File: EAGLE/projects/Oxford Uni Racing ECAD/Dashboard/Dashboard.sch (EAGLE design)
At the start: 21 parts, among them J1 T821108A1S100CEU, J2 CAN_OUT, J3 PWR_CAN, J4 DISPL, J6 BUTTONS, J7 BUTTONS, K1 EC2-12NU, K2 EC2-12NU, X2 D-SUB9-H2M09ST

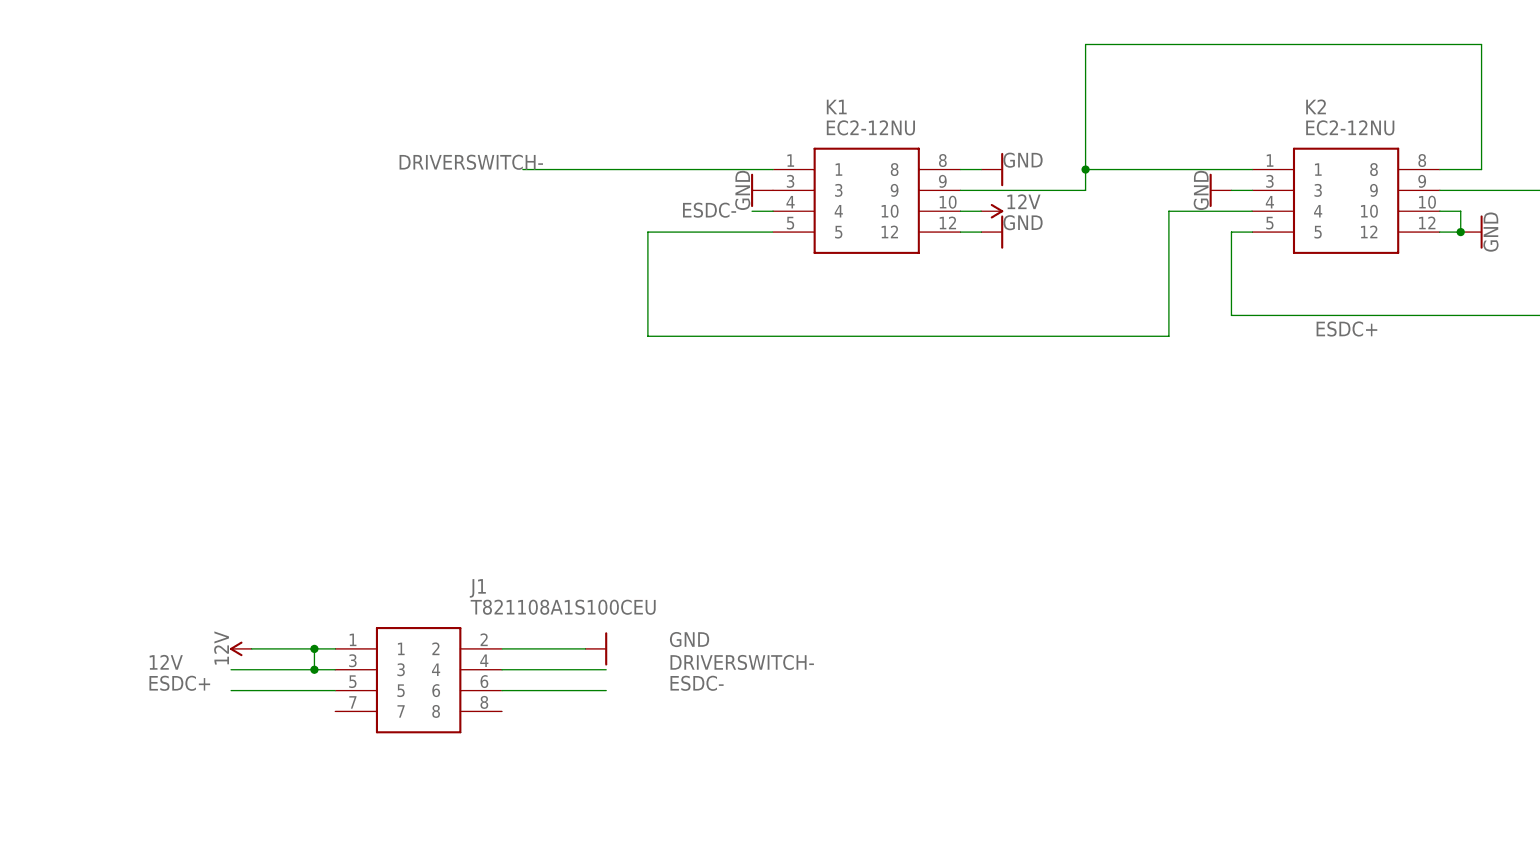
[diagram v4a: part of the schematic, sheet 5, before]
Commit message: fixed wiring of TS_Latch on dashboard
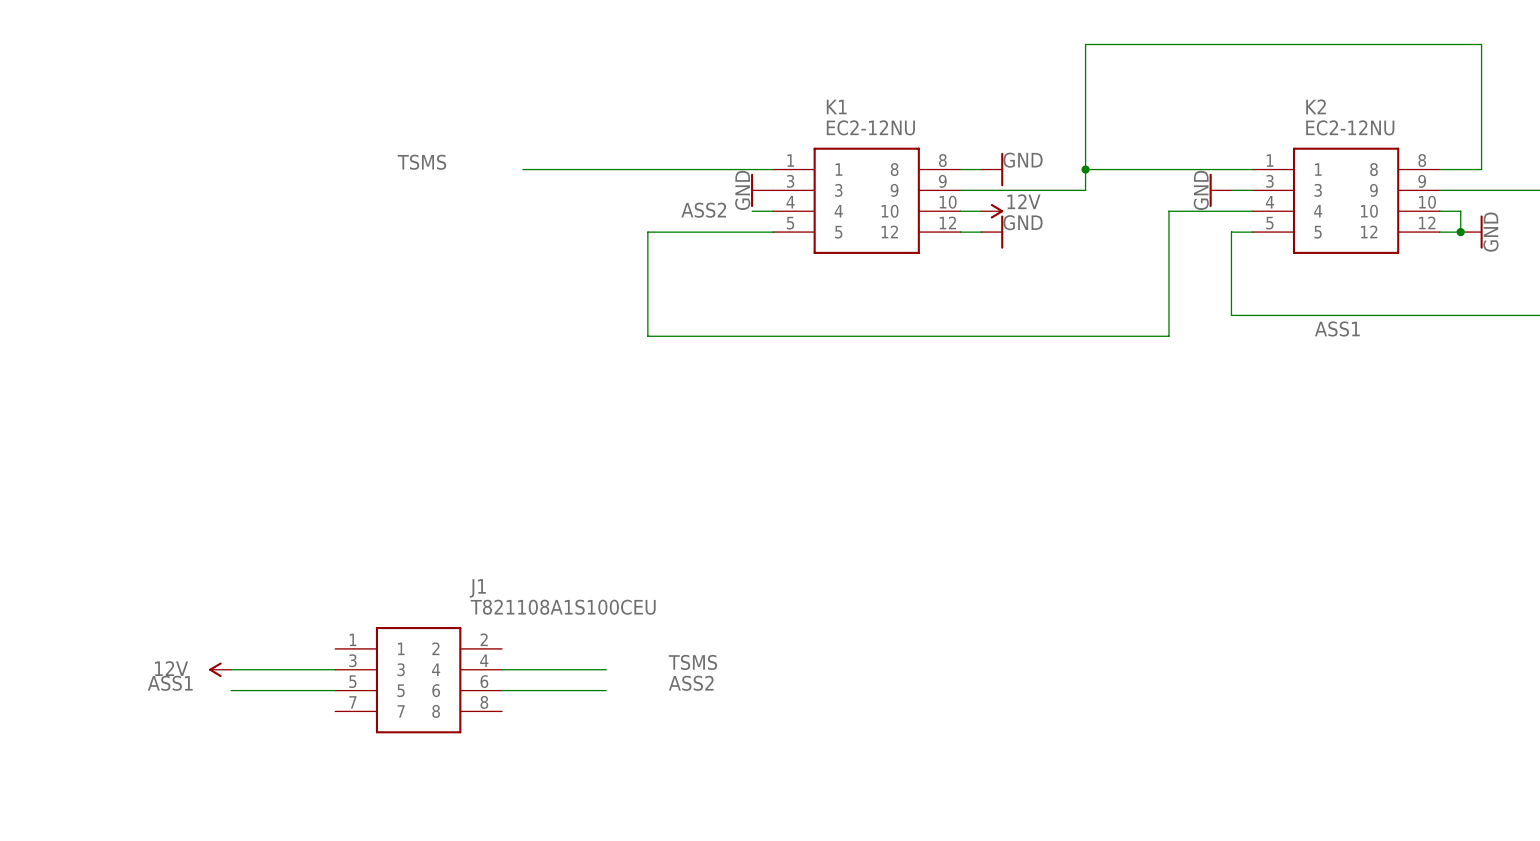
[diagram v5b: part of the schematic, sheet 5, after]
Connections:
- net DRIVERSWITCH- renamed TSMS
- net ESDC+ renamed ASS1
- net ESDC- renamed ASS2
- net 12V: no longer J1.1
- net GND: no longer J1.2
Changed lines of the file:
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@@
 <part name="GND12" library="SparkFun-PowerSymbols" library_urn="urn:adsk.eagle:library:530" deviceset="GND" device=""/>
 <part name="GND13" library="SparkFun-PowerSymbols" library_urn="urn:adsk.eagle:library:530" deviceset="GND" device=""/>
-<part name="GND14" library="SparkFun-PowerSymbols" library_urn="urn:adsk.eagle:library:530" deviceset="GND" device=""/>
-<part name="SUPPLY33" library="SparkFun-PowerSymbols" library_urn="urn:adsk.eagle:library:530" deviceset="12V" device=""/>
 <part name="SUPPLY1" library="SparkFun-PowerSymbols" library_urn="urn:adsk.eagle:library:530" deviceset="12V" device=""/>
 <part name="X2" library="con-thomas-betts" library_urn="urn:adsk.eagle:library:191" deviceset="D-SUB9-" device="H2M09ST" package3d_urn="urn:adsk.eagle:package:10567/1"/>
@@
 <part name="SUPPLY19" library="SparkFun-PowerSymbols" library_urn="urn:adsk.eagle:library:530" deviceset="3.3V" device=""/>
 <part name="GND4" library="SparkFun-PowerSymbols" library_urn="urn:adsk.eagle:library:530" deviceset="GND" device=""/>
+<part name="SUPPLY33" library="SparkFun-PowerSymbols" library_urn="urn:adsk.eagle:library:530" deviceset="12V" device=""/>
 </parts>
 <sheets>
@@
 <attribute name="VALUE" x="178.054" y="81.28" size="1.778" layer="96" rot="R90" align="top-center"/>
 </instance>
-<instance part="GND14" gate="1" x="71.12" y="30.48" smashed="yes" rot="R90">
-<attribute name="VALUE" x="81.28" y="30.734" size="1.778" layer="96" rot="R180" align="top-center"/>
-</instance>
-<instance part="SUPPLY33" gate="G$1" x="27.94" y="30.48" smashed="yes" rot="R90">
-<attribute name="VALUE" x="25.146" y="30.48" size="1.778" layer="96" rot="R90" align="bottom-center"/>
-</instance>
 <instance part="SUPPLY1" gate="G$1" x="116.84" y="83.82" smashed="yes" rot="R270">
 <attribute name="VALUE" x="121.92" y="84.074" size="1.778" layer="96" align="bottom-center"/>
@@
 <instance part="GND5" gate="1" x="-27.94" y="91.44" smashed="yes" rot="R90">
 <attribute name="VALUE" x="-27.686" y="91.44" size="1.778" layer="96" rot="R90" align="top-center"/>
+</instance>
+<instance part="SUPPLY33" gate="G$1" x="25.4" y="27.94" smashed="yes" rot="R90">
+<attribute name="VALUE" x="18.034" y="28.956" size="1.778" layer="96" rot="R180" align="bottom-center"/>
 </instance>
 </instances>
@@
 </segment>
 <segment>
-<pinref part="J1" gate="G$1" pin="2"/>
-<wire x1="58.42" y1="30.48" x2="68.58" y2="30.48" width="0.1524" layer="91"/>
-<pinref part="GND14" gate="1" pin="GND"/>
-</segment>
-<segment>
 <label x="-58.42" y="91.44" size="1.778" layer="95"/>
 <pinref part="GND5" gate="1" pin="GND"/>
 <wire x1="-30.48" y1="91.44" x2="-68.58" y2="91.44" width="0.1524" layer="91"/>
-</segment>
-</net>
-<net name="DRIVERSWITCH-" class="0">
-<segment>
-<pinref part="J1" gate="G$1" pin="4"/>
-<wire x1="58.42" y1="27.94" x2="71.12" y2="27.94" width="0.1524" layer="91"/>
-<label x="78.74" y="27.94" size="1.778" layer="95"/>
-</segment>
-<segment>
-<label x="45.72" y="88.9" size="1.778" layer="95"/>
-<pinref part="K1" gate="G$1" pin="1"/>
-<wire x1="60.96" y1="88.9" x2="91.44" y2="88.9" width="0.1524" layer="91"/>
-</segment>
-</net>
-<net name="ESDC+" class="0">
-<segment>
-<pinref part="J1" gate="G$1" pin="5"/>
-<wire x1="38.1" y1="25.4" x2="25.4" y2="25.4" width="0.1524" layer="91"/>
-<label x="15.24" y="25.4" size="1.778" layer="95"/>
-</segment>
-<segment>
-<pinref part="K2" gate="G$1" pin="5"/>
-<wire x1="149.86" y1="81.28" x2="147.32" y2="81.28" width="0.1524" layer="91"/>
-<label x="157.48" y="68.58" size="1.778" layer="95"/>
-<pinref part="K2" gate="G$1" pin="9"/>
-<wire x1="172.72" y1="86.36" x2="193.04" y2="86.36" width="0.1524" layer="91"/>
-<wire x1="193.04" y1="86.36" x2="193.04" y2="71.12" width="0.1524" layer="91"/>
-<wire x1="193.04" y1="71.12" x2="147.32" y2="71.12" width="0.1524" layer="91"/>
-<wire x1="147.32" y1="71.12" x2="147.32" y2="81.28" width="0.1524" layer="91"/>
-</segment>
-</net>
-<net name="ESDC-" class="0">
-<segment>
-<pinref part="J1" gate="G$1" pin="6"/>
-<wire x1="58.42" y1="25.4" x2="71.12" y2="25.4" width="0.1524" layer="91"/>
-<label x="78.74" y="25.4" size="1.778" layer="95"/>
-</segment>
-<segment>
-<pinref part="K1" gate="G$1" pin="4"/>
-<wire x1="91.44" y1="83.82" x2="88.9" y2="83.82" width="0.1524" layer="91"/>
-<label x="80.264" y="83.058" size="1.778" layer="95"/>
 </segment>
 </net>
@@
 </segment>
 <segment>
-<pinref part="J1" gate="G$1" pin="1"/>
-<wire x1="27.94" y1="30.48" x2="35.56" y2="30.48" width="0.1524" layer="91"/>
-<pinref part="J1" gate="G$1" pin="3"/>
-<wire x1="35.56" y1="30.48" x2="38.1" y2="30.48" width="0.1524" layer="91"/>
-<wire x1="38.1" y1="27.94" x2="35.56" y2="27.94" width="0.1524" layer="91"/>
-<label x="15.24" y="27.94" size="1.778" layer="95"/>
-<wire x1="35.56" y1="27.94" x2="25.4" y2="27.94" width="0.1524" layer="91"/>
-<wire x1="35.56" y1="30.48" x2="35.56" y2="27.94" width="0.1524" layer="91"/>
-<junction x="35.56" y="30.48"/>
-<junction x="35.56" y="27.94"/>
-<pinref part="SUPPLY33" gate="G$1" pin="12V"/>
-</segment>
-<segment>
 <label x="-58.42" y="99.06" size="1.778" layer="95"/>
 <pinref part="SUPPLY21" gate="G$1" pin="12V"/>
 <wire x1="-45.72" y1="99.06" x2="-68.58" y2="99.06" width="0.1524" layer="91"/>
 </segment>
+<segment>
+<pinref part="J1" gate="G$1" pin="3"/>
+<pinref part="SUPPLY33" gate="G$1" pin="12V"/>
+<wire x1="38.1" y1="27.94" x2="25.4" y2="27.94" width="0.1524" layer="91"/>
+</segment>
 </net>
 <net name="PWR_REDUCTION" class="0">
@@
 <wire x1="-58.42" y1="78.74" x2="-68.58" y2="78.74" width="0.1524" layer="91"/>
 </segment>
+<segment>
+<pinref part="J1" gate="G$1" pin="5"/>
+<wire x1="38.1" y1="25.4" x2="25.4" y2="25.4" width="0.1524" layer="91"/>
+<label x="15.24" y="25.4" size="1.778" layer="95"/>
+</segment>
+<segment>
+<pinref part="K2" gate="G$1" pin="5"/>
+<wire x1="149.86" y1="81.28" x2="147.32" y2="81.28" width="0.1524" layer="91"/>
+<label x="157.48" y="68.58" size="1.778" layer="95"/>
+<pinref part="K2" gate="G$1" pin="9"/>
+<wire x1="172.72" y1="86.36" x2="193.04" y2="86.36" width="0.1524" layer="91"/>
+<wire x1="193.04" y1="86.36" x2="193.04" y2="71.12" width="0.1524" layer="91"/>
+<wire x1="193.04" y1="71.12" x2="147.32" y2="71.12" width="0.1524" layer="91"/>
+<wire x1="147.32" y1="71.12" x2="147.32" y2="81.28" width="0.1524" layer="91"/>
+</segment>
 </net>
 <net name="ASS2" class="0">
@@
 <wire x1="-58.42" y1="76.2" x2="-68.58" y2="76.2" width="0.1524" layer="91"/>
 </segment>
+<segment>
+<pinref part="J1" gate="G$1" pin="6"/>
+<wire x1="58.42" y1="25.4" x2="71.12" y2="25.4" width="0.1524" layer="91"/>
+<label x="78.74" y="25.4" size="1.778" layer="95"/>
+</segment>
+<segment>
+<pinref part="K1" gate="G$1" pin="4"/>
+<wire x1="91.44" y1="83.82" x2="88.9" y2="83.82" width="0.1524" layer="91"/>
+<label x="80.264" y="83.058" size="1.778" layer="95"/>
+</segment>
 </net>
 <net name="SCK" class="0">
@@
 <wire x1="-58.42" y1="30.48" x2="-68.58" y2="30.48" width="0.1524" layer="91"/>
 </segment>
-</net>
+<segment>
+<pinref part="J1" gate="G$1" pin="4"/>
+<wire x1="58.42" y1="27.94" x2="71.12" y2="27.94" width="0.1524" layer="91"/>
+<label x="78.74" y="27.94" size="1.778" layer="95"/>
+</segment>
+<segment>
+<label x="45.72" y="88.9" size="1.778" layer="95"/>
+<pinref part="K1" gate="G$1" pin="1"/>
+<wire x1="60.96" y1="88.9" x2="91.44" y2="88.9" width="0.1524" layer="91"/>
+</segment>
+</net>

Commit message: finilised ASS details
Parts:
- added F1: 1A, fuse:FUSEBLANK_5X20MM
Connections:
- net TSMS renamed TRACTIVE_SYSTEM
- new net N$1: F1.1, J3.1, J3.2
- net 12V: now also F1.2; no longer J3.1, J3.2
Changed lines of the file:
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@@
 <part name="SUPPLY1" library="SparkFun-PowerSymbols" library_urn="urn:adsk.eagle:library:530" deviceset="12V" device=""/>
 <part name="X2" library="con-thomas-betts" library_urn="urn:adsk.eagle:library:191" deviceset="D-SUB9-" device="H2M09ST" package3d_urn="urn:adsk.eagle:package:10567/1"/>
-<part name="SUPPLY5" library="SparkFun-PowerSymbols" library_urn="urn:adsk.eagle:library:530" deviceset="12V" device=""/>
 <part name="GND18" library="SparkFun-PowerSymbols" library_urn="urn:adsk.eagle:library:530" deviceset="GND" device=""/>
 <part name="SUPPLY6" library="SparkFun-PowerSymbols" library_urn="urn:adsk.eagle:library:530" deviceset="5V" device=""/>
@@
 <part name="GND4" library="SparkFun-PowerSymbols" library_urn="urn:adsk.eagle:library:530" deviceset="GND" device=""/>
 <part name="SUPPLY33" library="SparkFun-PowerSymbols" library_urn="urn:adsk.eagle:library:530" deviceset="12V" device=""/>
+<part name="F1" library="fuse" library_urn="urn:adsk.eagle:library:233" deviceset="FUSE" device="BLANK_5X20MM" package3d_urn="urn:adsk.eagle:package:14079/1" value="1A"/>
 </parts>
 <sheets>
@@
 </segment>
 </net>
-<net name="TSMS" class="0">
+<net name="TRACTIVE_SYSTEM" class="0">
 <segment>
 <label x="10.16" y="20.32" size="1.778" layer="95"/>
@@
 <attribute name="NAME" x="118.11" y="60.198" size="1.778" layer="95"/>
 </instance>
-<instance part="SUPPLY5" gate="G$1" x="195.58" y="86.36" smashed="yes" rot="R270">
-<attribute name="VALUE" x="198.374" y="86.36" size="1.778" layer="96" rot="R270" align="bottom-center"/>
-</instance>
 <instance part="GND18" gate="1" x="198.12" y="81.28" smashed="yes" rot="R90">
 <attribute name="VALUE" x="198.374" y="81.28" size="1.778" layer="96" rot="R90" align="top-center"/>
@@
 <attribute name="VALUE" x="93.726" y="73.66" size="1.778" layer="96" rot="R270" align="top-center"/>
 </instance>
-<instance part="SUPPLY7" gate="G$1" x="152.4" y="86.36" smashed="yes" rot="R90">
-<attribute name="VALUE" x="149.606" y="86.36" size="1.778" layer="96" rot="R90" align="bottom-center"/>
+<instance part="SUPPLY7" gate="G$1" x="172.72" y="116.84" smashed="yes">
+<attribute name="VALUE" x="172.72" y="119.634" size="1.778" layer="96" align="bottom-center"/>
 </instance>
 <instance part="GND20" gate="1" x="147.32" y="81.28" smashed="yes" rot="R270">
@@
 <instance part="GND2" gate="1" x="40.64" y="81.28" smashed="yes" rot="R90">
 <attribute name="VALUE" x="40.894" y="81.28" size="1.778" layer="96" rot="R90" align="top-center"/>
+</instance>
+<instance part="F1" gate="G$1" x="172.72" y="104.14" smashed="yes" rot="R90">
+<attribute name="NAME" x="171.323" y="100.33" size="1.778" layer="95" rot="R90"/>
+<attribute name="VALUE" x="175.641" y="100.33" size="1.778" layer="96" rot="R90"/>
 </instance>
 </instances>
@@
 <net name="12V" class="0">
 <segment>
-<wire x1="162.56" y1="83.82" x2="157.48" y2="83.82" width="0.1524" layer="91"/>
-<wire x1="157.48" y1="83.82" x2="157.48" y2="86.36" width="0.1524" layer="91"/>
-<pinref part="SUPPLY7" gate="G$1" pin="12V"/>
-<wire x1="157.48" y1="86.36" x2="152.4" y2="86.36" width="0.1524" layer="91"/>
-<pinref part="J3" gate="G$1" pin="1"/>
-</segment>
-<segment>
-<wire x1="182.88" y1="83.82" x2="187.96" y2="83.82" width="0.1524" layer="91"/>
-<wire x1="187.96" y1="83.82" x2="187.96" y2="86.36" width="0.1524" layer="91"/>
-<pinref part="SUPPLY5" gate="G$1" pin="12V"/>
-<wire x1="187.96" y1="86.36" x2="195.58" y2="86.36" width="0.1524" layer="91"/>
-<pinref part="J3" gate="G$1" pin="2"/>
-</segment>
-<segment>
 <label x="10.16" y="88.9" size="1.778" layer="95"/>
 <pinref part="SUPPLY12" gate="G$1" pin="12V"/>
 <wire x1="22.86" y1="88.9" x2="0" y2="88.9" width="0.1524" layer="91"/>
+</segment>
+<segment>
+<pinref part="F1" gate="G$1" pin="2"/>
+<pinref part="SUPPLY7" gate="G$1" pin="12V"/>
+<wire x1="172.72" y1="109.22" x2="172.72" y2="116.84" width="0.1524" layer="91"/>
 </segment>
 </net>
@@
 </segment>
 </net>
-<net name="TSMS" class="0">
+<net name="TRACTIVE_SYSTEM" class="0">
 <segment>
 <label x="10.16" y="20.32" size="1.778" layer="95"/>
@@
 <label x="10.16" y="33.02" size="1.778" layer="95"/>
 <wire x1="10.16" y1="33.02" x2="0" y2="33.02" width="0.1524" layer="91"/>
+</segment>
+</net>
+<net name="N$1" class="0">
+<segment>
+<wire x1="162.56" y1="83.82" x2="157.48" y2="83.82" width="0.1524" layer="91"/>
+<pinref part="J3" gate="G$1" pin="1"/>
+<wire x1="157.48" y1="83.82" x2="157.48" y2="93.98" width="0.1524" layer="91"/>
+<wire x1="157.48" y1="93.98" x2="172.72" y2="93.98" width="0.1524" layer="91"/>
+<wire x1="172.72" y1="93.98" x2="187.96" y2="93.98" width="0.1524" layer="91"/>
+<wire x1="182.88" y1="83.82" x2="187.96" y2="83.82" width="0.1524" layer="91"/>
+<pinref part="J3" gate="G$1" pin="2"/>
+<wire x1="187.96" y1="93.98" x2="187.96" y2="83.82" width="0.1524" layer="91"/>
+<pinref part="F1" gate="G$1" pin="1"/>
+<wire x1="172.72" y1="93.98" x2="172.72" y2="99.06" width="0.1524" layer="91"/>
+<junction x="172.72" y="93.98"/>
 </segment>
 </net>
@@
 </segment>
 </net>
-<net name="TSMS" class="0">
+<net name="TRACTIVE_SYSTEM" class="0">
 <segment>
 <label x="10.16" y="20.32" size="1.778" layer="95"/>
@@
 </segment>
 </net>
-<net name="TSMS" class="0">
+<net name="TRACTIVE_SYSTEM" class="0">
 <segment>
 <label x="10.16" y="20.32" size="1.778" layer="95"/>
@@
 </segment>
 </net>
-<net name="TSMS" class="0">
+<net name="TRACTIVE_SYSTEM" class="0">
 <segment>
 <label x="-58.42" y="30.48" size="1.778" layer="95"/>
@@
 </segment>
 </net>
-<net name="TSMS" class="0">
+<net name="TRACTIVE_SYSTEM" class="0">
 <segment>
 <label x="10.16" y="20.32" size="1.778" layer="95"/>
@@
 </segment>
 </net>
-<net name="TSMS" class="0">
+<net name="TRACTIVE_SYSTEM" class="0">
 <segment>
 <label x="10.16" y="20.32" size="1.778" layer="95"/>
@@
 </segment>
 </net>
-<net name="TSMS" class="0">
+<net name="TRACTIVE_SYSTEM" class="0">
 <segment>
 <label x="10.16" y="20.32" size="1.778" layer="95"/>

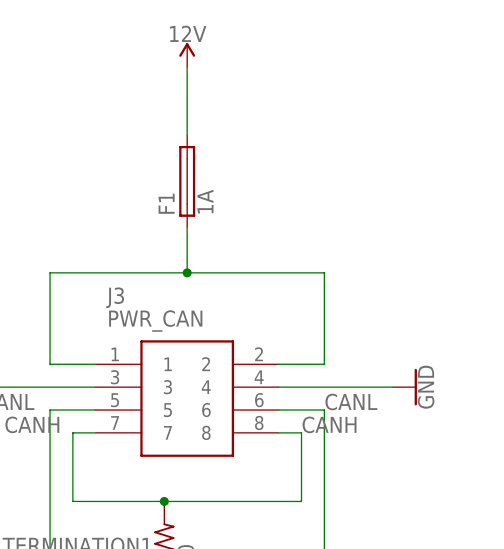
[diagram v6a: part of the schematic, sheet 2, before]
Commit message: added fuses to boards
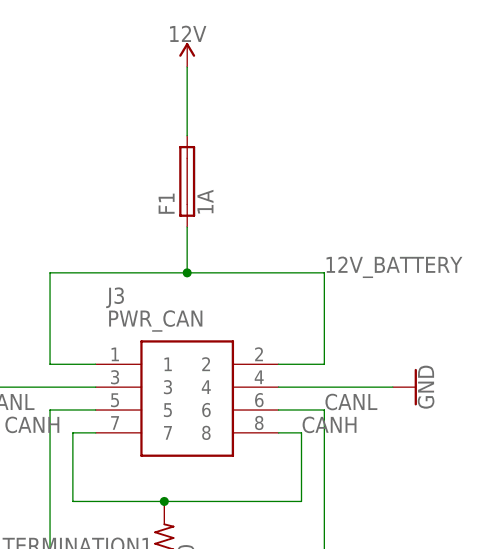
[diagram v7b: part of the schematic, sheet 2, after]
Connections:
- net N$1 renamed 12V_BATTERY
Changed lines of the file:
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@@
 </segment>
 </net>
-<net name="N$1" class="0">
+<net name="12V_BATTERY" class="0">
 <segment>
 <wire x1="162.56" y1="83.82" x2="157.48" y2="83.82" width="0.1524" layer="91"/>
@@
 <wire x1="172.72" y1="93.98" x2="172.72" y2="99.06" width="0.1524" layer="91"/>
 <junction x="172.72" y="93.98"/>
+<label x="187.96" y="93.98" size="1.778" layer="95"/>
 </segment>
 </net>
